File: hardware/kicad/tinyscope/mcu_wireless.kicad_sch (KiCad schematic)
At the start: 9 parts, among them J4 MDBT50Q_TAG_CONNECT, U11 MDBT50Q-1MV2, X1 32k768

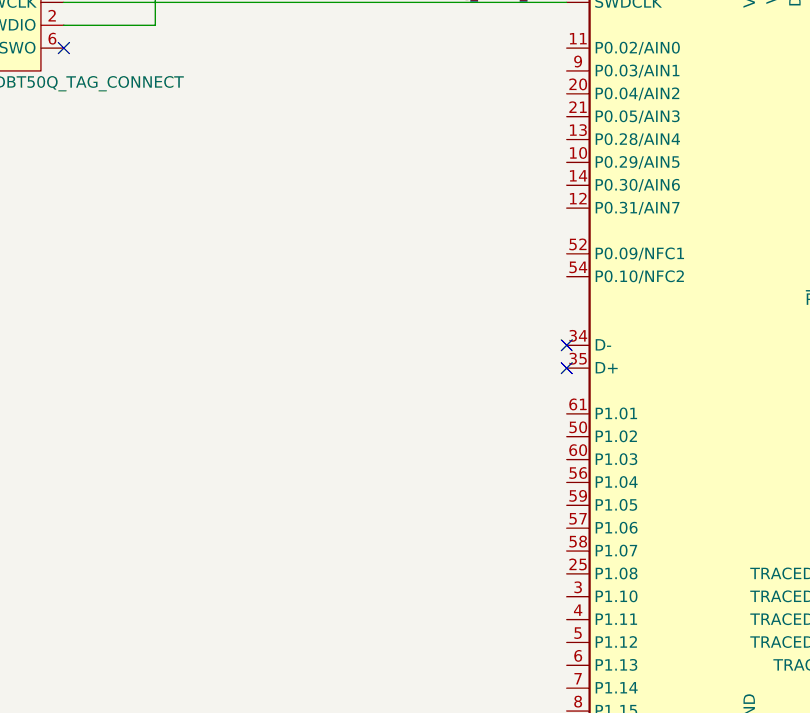
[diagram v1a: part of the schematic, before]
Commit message: feat: hardware: Adds blue led mosfet driver for MDBT50Q
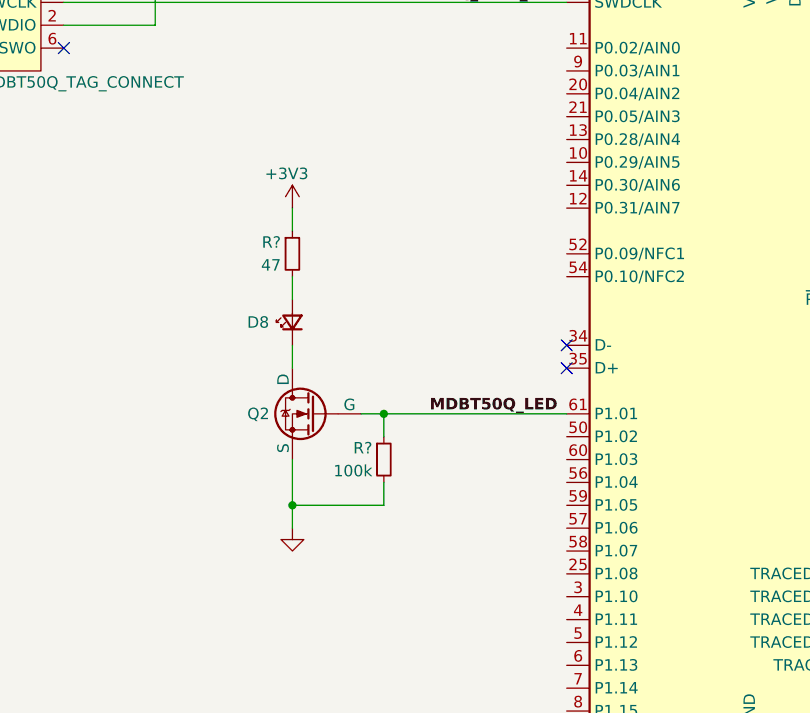
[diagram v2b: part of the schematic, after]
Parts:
- added D8: Blue, symbol Device:LED_Small
- added Q2: NMOS, symbol Simulation_SPICE:NMOS
- added R?: 47, symbol Device:R_Small
- added R?: 100k, symbol Device:R_Small
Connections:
- net +3V3: now also R?.1
- net GND: now also Q2.3 (S), R?.2
- net MDBT50Q_LED: now reaches U11.61 (P1.01)
- net MDBT50Q_LED: now also Q2.2 (G), R?.1
- new net: D8.2 (A), R?.2
- new net: D8.1 (K), Q2.1 (D)
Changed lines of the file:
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@@
     (rev "v0.1")
   )
+  (junction (at 99.06 93.98) (diameter 0) (color 0 0 0 0)
+  )
   (junction (at 187.96 55.88) (diameter 0) (color 0 0 0 0)
   )
@@
   )
   (junction (at 172.72 48.26) (diameter 0) (color 0 0 0 0)
+  )
+  (junction (at 88.9 104.14) (diameter 0) (color 0 0 0 0)
   )
   (no_connect (at 63.5 53.34))
@@
     (stroke (width 0) (type default))
   )
+  (wire (pts (xy 88.9 104.14) (xy 99.06 104.14))
+    (stroke (width 0) (type default))
+  )
+  (wire (pts (xy 88.9 78.74) (xy 88.9 81.28))
+    (stroke (width 0) (type default))
+  )
+  (wire (pts (xy 88.9 99.06) (xy 88.9 104.14))
+    (stroke (width 0) (type default))
+  )
+  (wire (pts (xy 88.9 86.36) (xy 88.9 88.9))
+    (stroke (width 0) (type default))
+  )
+  (wire (pts (xy 88.9 71.12) (xy 88.9 73.66))
+    (stroke (width 0) (type default))
+  )
+  (wire (pts (xy 99.06 93.98) (xy 119.38 93.98))
+    (stroke (width 0) (type default))
+  )
   (wire (pts (xy 106.68 22.86) (xy 116.84 22.86))
     (stroke (width 0) (type default))
   )
+  (wire (pts (xy 88.9 104.14) (xy 88.9 106.68))
+    (stroke (width 0) (type default))
+  )
   (wire (pts (xy 162.56 48.26) (xy 172.72 48.26))
     (stroke (width 0) (type default))
@@
     (stroke (width 0) (type default))
   )
+  (wire (pts (xy 96.52 93.98) (xy 99.06 93.98))
+    (stroke (width 0) (type default))
+  )
   (wire (pts (xy 53.34 35.56) (xy 53.34 38.1))
     (stroke (width 0) (type default))
@@
     (stroke (width 0) (type default))
   )
+  (wire (pts (xy 99.06 93.98) (xy 99.06 96.52))
+    (stroke (width 0) (type default))
+  )
   (wire (pts (xy 137.16 22.86) (xy 144.78 22.86))
     (stroke (width 0) (type default))
@@
   )
   (wire (pts (xy 160.02 50.8) (xy 162.56 50.8))
+    (stroke (width 0) (type default))
+  )
+  (wire (pts (xy 99.06 101.6) (xy 99.06 104.14))
     (stroke (width 0) (type default))
   )
@@
     (effects (font (size 1.27 1.27) bold) (justify right bottom))
   )
+  (label "MDBT50Q_LED" (at 104.14 93.98 0) (fields_autoplaced)
+    (effects (font (size 1.27 1.27) bold) (justify left bottom))
+  )
   (label "MDBT50Q_SWD_NRST" (at 182.88 81.28 180) (fields_autoplaced)
     (effects (font (size 1.27 1.27) bold) (justify right bottom))
@@
         (path "/bb072e32-cc57-415a-8554-0e84d374f333/8ab32ff2-1997-48a8-8f3b-8df038411955"
           (reference "R26") (unit 1)
+        )
+      )
+    )
+  )
+  (symbol (lib_id "Device:R_Small") (at 88.9 76.2 0) (unit 1)
+    (in_bom yes) (on_board yes) (dnp no)
+    (property "Reference" "R?" (at 87.63 74.93 0)
+      (effects (font (size 1.27 1.27)) (justify right))
+    )
+    (property "Value" "47" (at 87.63 77.47 0)
+      (effects (font (size 1.27 1.27)) (justify right))
+    )
+    (property "Footprint" "" (at 88.9 76.2 0)
+      (effects (font (size 1.27 1.27)) hide)
+    )
+    (property "Datasheet" "~" (at 88.9 76.2 0)
+      (effects (font (size 1.27 1.27)) hide)
+    )
+    (pin "1")
+    (pin "2")
+    (instances
+      (project "tinyscope"
+        (path "/bb072e32-cc57-415a-8554-0e84d374f333"
+          (reference "R?") (unit 1)
+        )
+        (path "/bb072e32-cc57-415a-8554-0e84d374f333/7c1b1425-60eb-4f71-b125-42ba246f39fb"
+          (reference "R10") (unit 1)
+        )
+        (path "/bb072e32-cc57-415a-8554-0e84d374f333/8ab32ff2-1997-48a8-8f3b-8df038411955"
+          (reference "R27") (unit 1)
         )
       )
@@
     )
   )
+  (symbol (lib_id "power:GND") (at 88.9 106.68 0) (mirror y) (unit 1)
+    (in_bom yes) (on_board yes) (dnp no) (fields_autoplaced)
+    (property "Reference" "#PWR?" (at 88.9 113.03 0)
+      (effects (font (size 1.27 1.27)) hide)
+    )
+    (property "Value" "GND" (at 88.9 111.76 0)
+      (effects (font (size 1.27 1.27)) hide)
+    )
+    (property "Footprint" "" (at 88.9 106.68 0)
+      (effects (font (size 1.27 1.27)) hide)
+    )
+    (property "Datasheet" "" (at 88.9 106.68 0)
+      (effects (font (size 1.27 1.27)) hide)
+    )
+    (pin "1")
+    (instances
+      (project "tinyscope"
+        (path "/bb072e32-cc57-415a-8554-0e84d374f333"
+          (reference "#PWR?") (unit 1)
+        )
+        (path "/bb072e32-cc57-415a-8554-0e84d374f333/1c26ba79-0794-42b8-82e1-265696d83365"
+          (reference "#PWR034") (unit 1)
+        )
+        (path "/bb072e32-cc57-415a-8554-0e84d374f333/f3c865ab-23cb-49a1-bb6d-4ee24e55c7fa"
+          (reference "#PWR045") (unit 1)
+        )
+        (path "/bb072e32-cc57-415a-8554-0e84d374f333/8ab32ff2-1997-48a8-8f3b-8df038411955"
+          (reference "#PWR068") (unit 1)
+        )
+      )
+    )
+  )
   (symbol (lib_id "power:+3V3") (at 106.68 20.32 0) (mirror y) (unit 1)
     (in_bom yes) (on_board yes) (dnp no)
@@
     )
   )
+  (symbol (lib_id "Device:LED_Small") (at 88.9 83.82 90) (unit 1)
+    (in_bom yes) (on_board yes) (dnp no)
+    (property "Reference" "D8" (at 85.09 83.82 90)
+      (effects (font (size 1.27 1.27)))
+    )
+    (property "Value" "Blue" (at 85.09 83.7565 0)
+      (effects (font (size 1.27 1.27)) hide)
+    )
+    (property "Footprint" "" (at 88.9 83.82 90)
+      (effects (font (size 1.27 1.27)) hide)
+    )
+    (property "Datasheet" "https://www.mouser.pl/ProductDetail/Dialight/599-0H90-147F?qs=sGAEpiMZZMvVL5Kk7ZYykY6g4CMvHY6uEiu%252BcrVUkqZ6q%2FNpyWJ2ww%3D%3D" (at 88.9 83.82 90)
+      (effects (font (size 1.27 1.27)) hide)
+    )
+    (pin "1")
+    (pin "2")
+    (instances
+      (project "tinyscope"
+        (path "/bb072e32-cc57-415a-8554-0e84d374f333/8ab32ff2-1997-48a8-8f3b-8df038411955"
+          (reference "D8") (unit 1)
+        )
+      )
+    )
+  )
   (symbol (lib_id "power:GND") (at 139.7 33.02 0) (mirror y) (unit 1)
     (in_bom yes) (on_board yes) (dnp no) (fields_autoplaced)
@@
     )
   )
+  (symbol (lib_id "Simulation_SPICE:NMOS") (at 91.44 93.98 0) (mirror y) (unit 1)
+    (in_bom yes) (on_board yes) (dnp no)
+    (property "Reference" "Q2" (at 86.36 93.98 0)
+      (effects (font (size 1.27 1.27)) (justify left))
+    )
+    (property "Value" "NMOS" (at 85.09 95.25 0)
+      (effects (font (size 1.27 1.27)) (justify left) hide)
+    )
+    (property "Footprint" "" (at 86.36 91.44 0)
+      (effects (font (size 1.27 1.27)) hide)
+    )
+    (property "Datasheet" "https://ngspice.sourceforge.io/docs/ngspice-manual.pdf" (at 91.44 106.68 0)
+      (effects (font (size 1.27 1.27)) hide)
+    )
+    (property "Sim.Device" "NMOS" (at 91.44 111.125 0)
+      (effects (font (size 1.27 1.27)) hide)
+    )
+    (property "Sim.Type" "VDMOS" (at 91.44 113.03 0)
+      (effects (font (size 1.27 1.27)) hide)
+    )
+    (property "Sim.Pins" "1=D 2=G 3=S" (at 91.44 109.22 0)
+      (effects (font (size 1.27 1.27)) hide)
+    )
+    (pin "1")
+    (pin "2")
+    (pin "3")
+    (instances
+      (project "tinyscope"
+        (path "/bb072e32-cc57-415a-8554-0e84d374f333/8ab32ff2-1997-48a8-8f3b-8df038411955"
+          (reference "Q2") (unit 1)
+        )
+      )
+    )
+  )
   (symbol (lib_id "power:+3V3") (at 53.34 35.56 0) (mirror y) (unit 1)
     (in_bom yes) (on_board yes) (dnp no)
@@
         )
       )
+    )
+  )
+  (symbol (lib_id "power:+3V3") (at 88.9 71.12 0) (mirror y) (unit 1)
+    (in_bom yes) (on_board yes) (dnp no)
+    (property "Reference" "#PWR041" (at 88.9 74.93 0)
+      (effects (font (size 1.27 1.27)) hide)
+    )
+    (property "Value" "+3V3" (at 88.265 67.31 0)
+      (effects (font (size 1.27 1.27)))
+    )
+    (property "Footprint" "" (at 88.9 71.12 0)
+      (effects (font (size 1.27 1.27)) hide)
+    )
+    (property "Datasheet" "" (at 88.9 71.12 0)
+      (effects (font (size 1.27 1.27)) hide)
+    )
+    (pin "1")
+    (instances
+      (project "tinyscope"
+        (path "/bb072e32-cc57-415a-8554-0e84d374f333/f3c865ab-23cb-49a1-bb6d-4ee24e55c7fa"
+          (reference "#PWR041") (unit 1)
+        )
+        (path "/bb072e32-cc57-415a-8554-0e84d374f333/8ab32ff2-1997-48a8-8f3b-8df038411955"
+          (reference "#PWR067") (unit 1)
+        )
+      )
+    )
+  )
+  (symbol (lib_id "Device:R_Small") (at 99.06 99.06 0) (unit 1)
+    (in_bom yes) (on_board yes) (dnp no)
+    (property "Reference" "R?" (at 97.79 97.79 0)
+      (effects (font (size 1.27 1.27)) (justify right))
+    )
+    (property "Value" "100k" (at 97.79 100.33 0)
+      (effects (font (size 1.27 1.27)) (justify right))
+    )
+    (property "Footprint" "" (at 99.06 99.06 0)
+      (effects (font (size 1.27 1.27)) hide)
+    )
+    (property "Datasheet" "~" (at 99.06 99.06 0)
+      (effects (font (size 1.27 1.27)) hide)
+    )
+    (pin "1")
+    (pin "2")
+    (instances
+      (project "tinyscope"
+        (path "/bb072e32-cc57-415a-8554-0e84d374f333"
+          (reference "R?") (unit 1)
+        )
+        (path "/bb072e32-cc57-415a-8554-0e84d374f333/7c1b1425-60eb-4f71-b125-42ba246f39fb"
+          (reference "R10") (unit 1)
+        )
+        (path "/bb072e32-cc57-415a-8554-0e84d374f333/8ab32ff2-1997-48a8-8f3b-8df038411955"
+          (reference "R28") (unit 1)
+        )
+      )

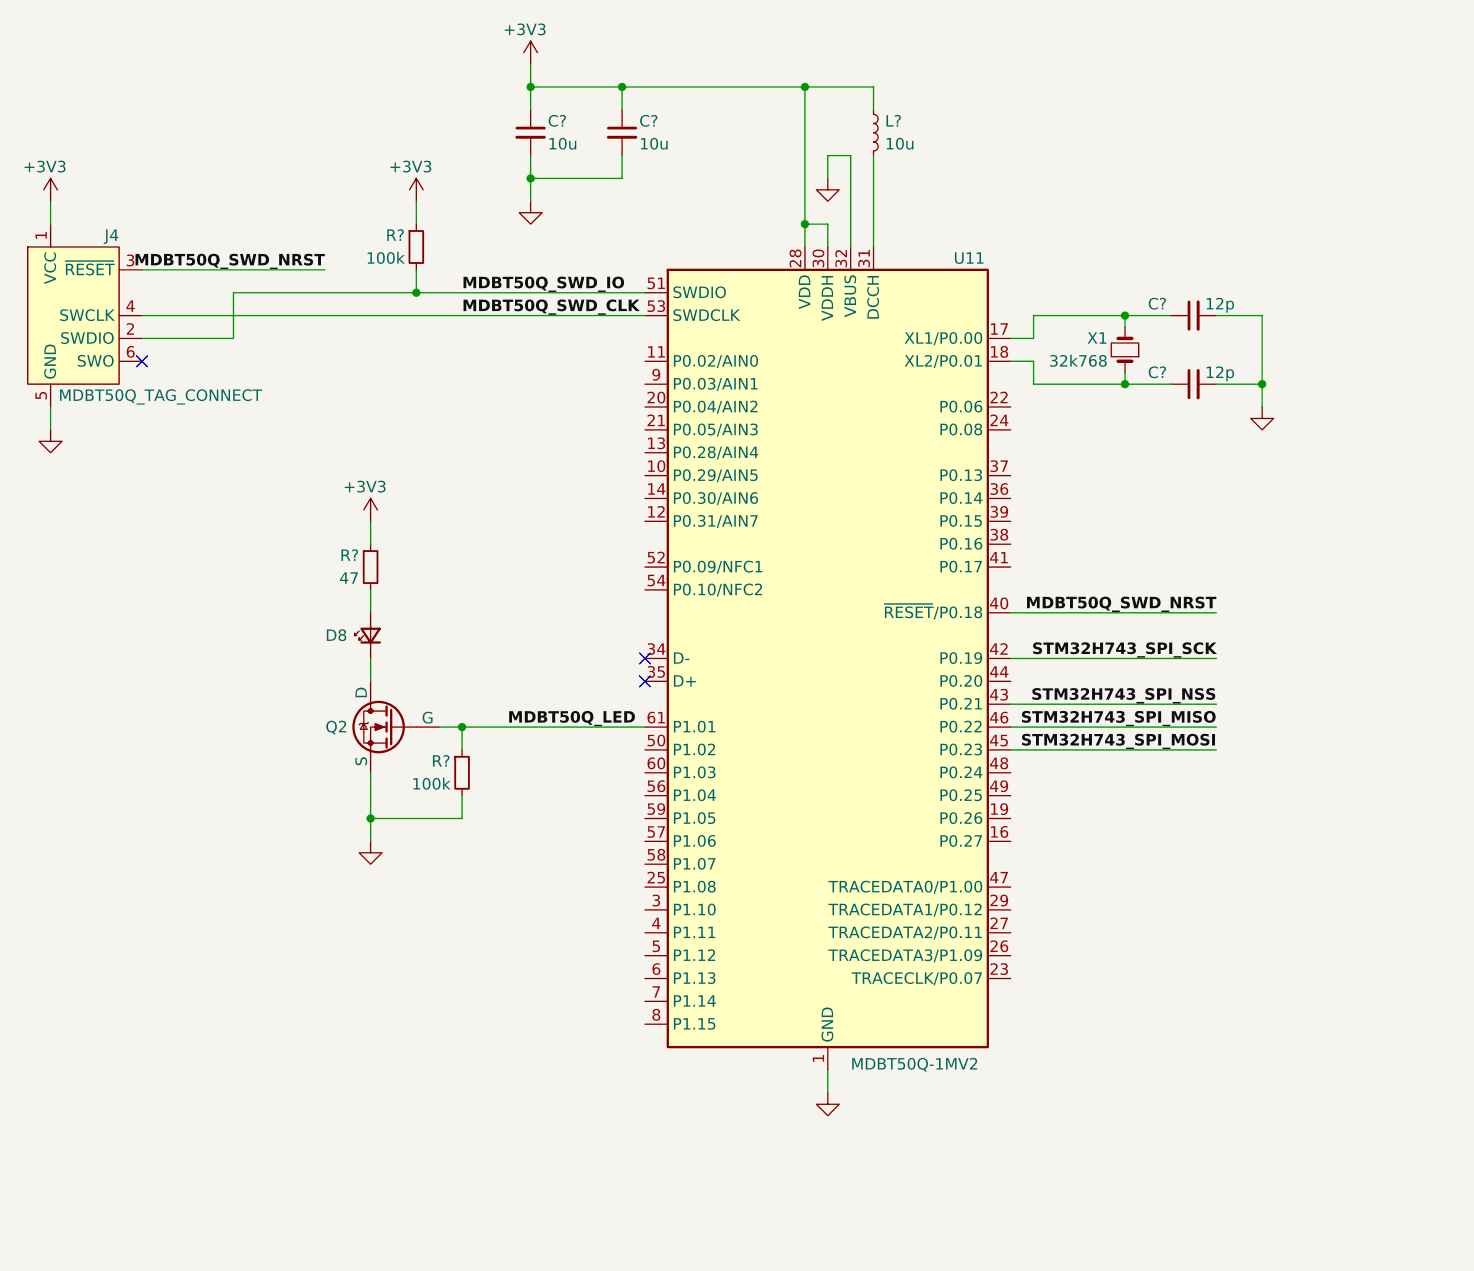
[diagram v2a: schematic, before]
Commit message: feat: hardware: Finish MCU wireless schematic
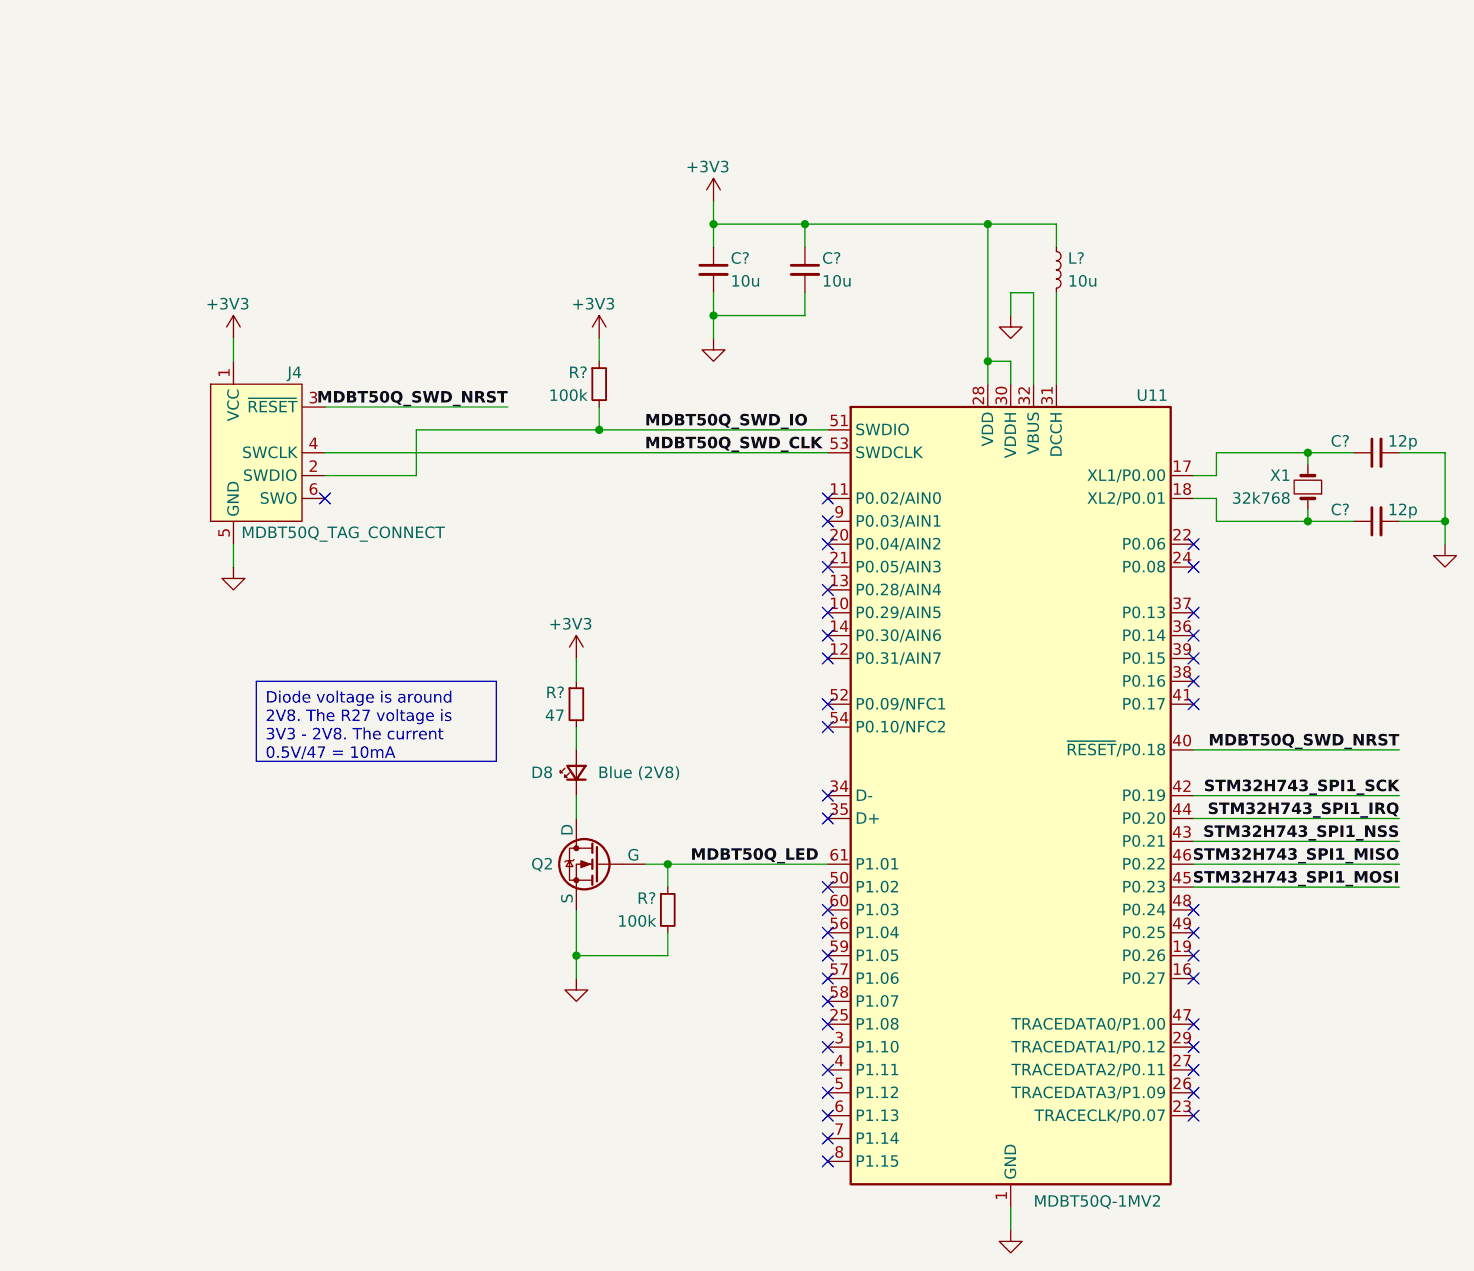
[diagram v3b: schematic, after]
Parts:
- D8: value Blue -> Blue (2V8)
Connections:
- net STM32H743_SPI1_IRQ: now reaches U11.44 (P0.20)
- net STM32H743_SPI_MISO renamed STM32H743_SPI1_MISO
- net STM32H743_SPI_MOSI renamed STM32H743_SPI1_MOSI
- net STM32H743_SPI_NSS renamed STM32H743_SPI1_NSS
- net STM32H743_SPI_SCK renamed STM32H743_SPI1_SCK
- no-connect marks 3 -> 42
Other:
- moved on the sheet: C?, D8, J4, L?, Q2, R?, U11, X1
